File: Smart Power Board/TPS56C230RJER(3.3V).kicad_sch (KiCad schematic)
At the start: 19 parts, among them U5 TPS56C230RJER

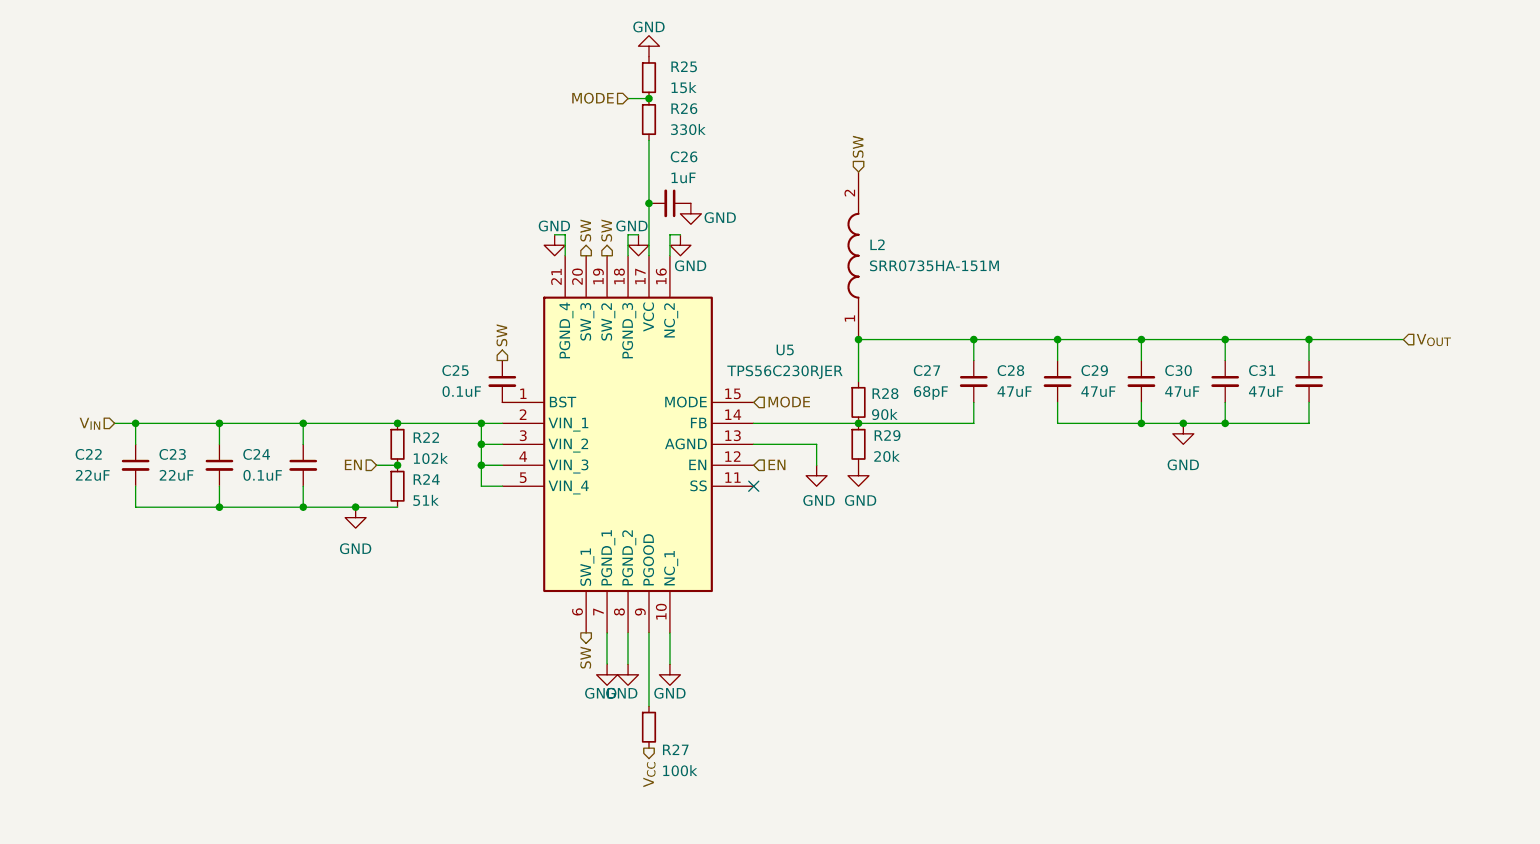
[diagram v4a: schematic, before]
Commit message: Feat[SmartPowerBoard]: Organized Schematic and New Buck
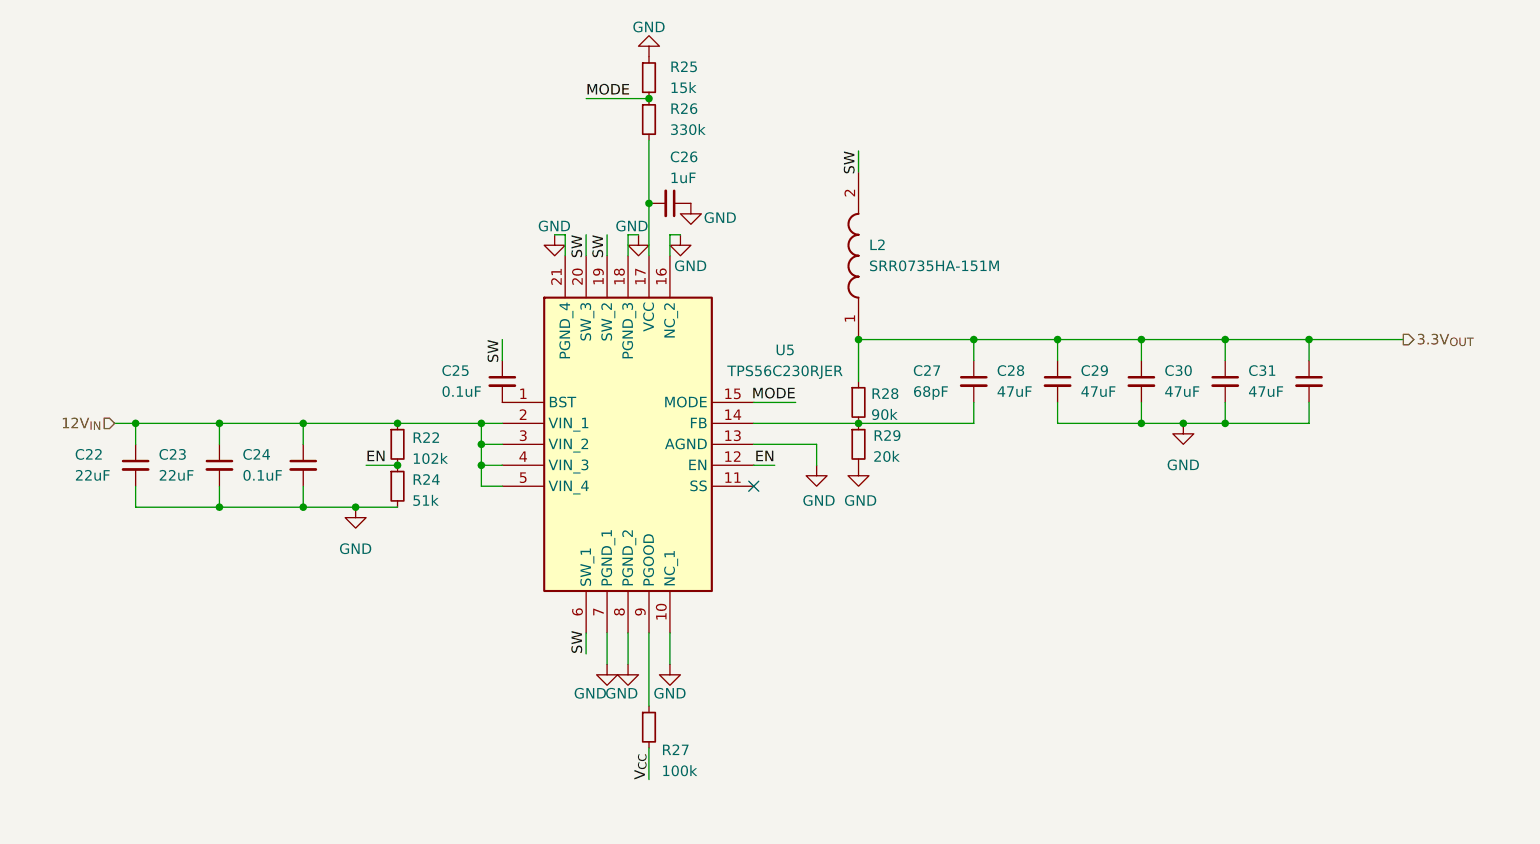
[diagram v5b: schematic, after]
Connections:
- net V_{IN} renamed 12V_{IN}
- net V_{OUT} renamed 3.3V_{OUT}
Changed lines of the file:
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@@
+	(wire
+		(pts
+			(xy 129.54 92.71) (xy 129.54 95.25)
+		)
+		(stroke
+			(width 0)
+			(type default)
+		)
+	)
 	(wire
 		(pts
@@
 	(wire
 		(pts
+			(xy 162.56 107.95) (xy 160.02 107.95)
+		)
+		(stroke
+			(width 0)
+			(type default)
+		)
+	)
+	(wire
+		(pts
 			(xy 142.24 128.27) (xy 142.24 132.08)
 		)
@@
 	(wire
 		(pts
-			(xy 144.78 63.5) (xy 147.32 63.5)
+			(xy 139.7 63.5) (xy 147.32 63.5)
 		)
 		(stroke
@@
 	(wire
 		(pts
+			(xy 165.1 100.33) (xy 160.02 100.33)
+		)
+		(stroke
+			(width 0)
+			(type default)
+		)
+	)
+	(wire
+		(pts
 			(xy 227.33 100.33) (xy 227.33 102.87)
 		)
@@
 	(wire
 		(pts
-			(xy 114.3 107.95) (xy 116.84 107.95)
+			(xy 113.03 107.95) (xy 116.84 107.95)
 		)
 		(stroke
@@
 	(wire
 		(pts
+			(xy 142.24 80.01) (xy 142.24 82.55)
+		)
+		(stroke
+			(width 0)
+			(type default)
+		)
+	)
+	(wire
+		(pts
+			(xy 139.7 80.01) (xy 139.7 82.55)
+		)
+		(stroke
+			(width 0)
+			(type default)
+		)
+	)
+	(wire
+		(pts
+			(xy 147.32 146.05) (xy 147.32 142.24)
+		)
+		(stroke
+			(width 0)
+			(type default)
+		)
+	)
+	(wire
+		(pts
 			(xy 196.85 100.33) (xy 196.85 102.87)
 		)
@@
 	(wire
 		(pts
+			(xy 139.7 130.81) (xy 139.7 128.27)
+		)
+		(stroke
+			(width 0)
+			(type default)
+		)
+	)
+	(wire
+		(pts
 			(xy 227.33 92.71) (xy 227.33 95.25)
 		)
@@
 	(wire
 		(pts
+			(xy 172.72 69.85) (xy 172.72 72.39)
+		)
+		(stroke
+			(width 0)
+			(type default)
+		)
+	)
+	(wire
+		(pts
 			(xy 137.16 80.01) (xy 137.16 82.55)
 		)
@@
 		)
 	)
-	(hierarchical_label "EN"
-		(shape input)
-		(at 114.3 107.95 180)
+	(label "SW"
+		(at 129.54 92.71 270)
 		(fields_autoplaced yes)
 		(effects
@@
 				(size 1.27 1.27)
 			)
-			(justify right)
-		)
-	)
-	(hierarchical_label "SW"
-		(shape input)
-		(at 172.72 72.39 90)
+			(justify right bottom)
+		)
+	)
+	(label "MODE"
+		(at 139.7 63.5 0)
 		(fields_autoplaced yes)
 		(effects
@@
 				(size 1.27 1.27)
 			)
-			(justify left)
-		)
-	)
-	(hierarchical_label "SW"
-		(shape output)
-		(at 139.7 82.55 90)
+			(justify left bottom)
+		)
+	)
+	(label "SW"
+		(at 142.24 80.01 270)
 		(fields_autoplaced yes)
 		(effects
@@
 				(size 1.27 1.27)
 			)
-			(justify left)
-		)
-	)
-	(hierarchical_label "EN"
-		(shape input)
-		(at 160.02 107.95 0)
+			(justify right bottom)
+		)
+	)
+	(label "SW"
+		(at 139.7 80.01 270)
 		(fields_autoplaced yes)
 		(effects
@@
 				(size 1.27 1.27)
 			)
-			(justify left)
-		)
-	)
-	(hierarchical_label "MODE"
-		(shape input)
-		(at 160.02 100.33 0)
+			(justify right bottom)
+		)
+	)
+	(label "SW"
+		(at 139.7 130.81 90)
 		(fields_autoplaced yes)
 		(effects
@@
 				(size 1.27 1.27)
 			)
-			(justify left)
-		)
-	)
-	(hierarchical_label "V_{CC}"
-		(shape output)
-		(at 147.32 142.24 270)
+			(justify left bottom)
+		)
+	)
+	(label "EN"
+		(at 162.56 107.95 180)
 		(fields_autoplaced yes)
 		(effects
@@
 				(size 1.27 1.27)
 			)
-			(justify right)
-		)
-	)
-	(hierarchical_label "MODE"
-		(shape input)
-		(at 144.78 63.5 180)
+			(justify right bottom)
+		)
+	)
+	(label "MODE"
+		(at 165.1 100.33 180)
 		(fields_autoplaced yes)
 		(effects
@@
 				(size 1.27 1.27)
 			)
-			(justify right)
-		)
-	)
-	(hierarchical_label "SW"
-		(shape output)
-		(at 129.54 95.25 90)
+			(justify right bottom)
+		)
+	)
+	(label "EN"
+		(at 113.03 107.95 0)
 		(fields_autoplaced yes)
 		(effects
@@
 				(size 1.27 1.27)
 			)
-			(justify left)
-		)
-	)
-	(hierarchical_label "SW"
-		(shape output)
-		(at 139.7 128.27 270)
+			(justify left bottom)
+		)
+	)
+	(label "V_{CC}"
+		(at 147.32 146.05 90)
 		(fields_autoplaced yes)
 		(effects
@@
 				(size 1.27 1.27)
 			)
-			(justify right)
-		)
-	)
-	(hierarchical_label "V_{IN}"
+			(justify left bottom)
+		)
+	)
+	(label "SW"
+		(at 172.72 69.85 270)
+		(fields_autoplaced yes)
+		(effects
+			(font
+				(size 1.27 1.27)
+			)
+			(justify right bottom)
+		)
+	)
+	(hierarchical_label "12V_{IN}"
 		(shape input)
 		(at 82.55 102.87 180)
@@
 		)
 	)
-	(hierarchical_label "V_{OUT}"
-		(shape input)
+	(hierarchical_label "3.3V_{OUT}"
+		(shape output)
 		(at 238.76 92.71 0)
-		(fields_autoplaced yes)
-		(effects
-			(font
-				(size 1.27 1.27)
-			)
-			(justify left)
-		)
-	)
-	(hierarchical_label "SW"
-		(shape output)
-		(at 142.24 82.55 90)
 		(fields_autoplaced yes)
 		(effects
@@
 		)
 		(property "Value" "GND"
-			(at 141.478 135.636 0)
-			(effects
-				(font
+			(at 140.208 135.636 0)
+			(effects
+				(font

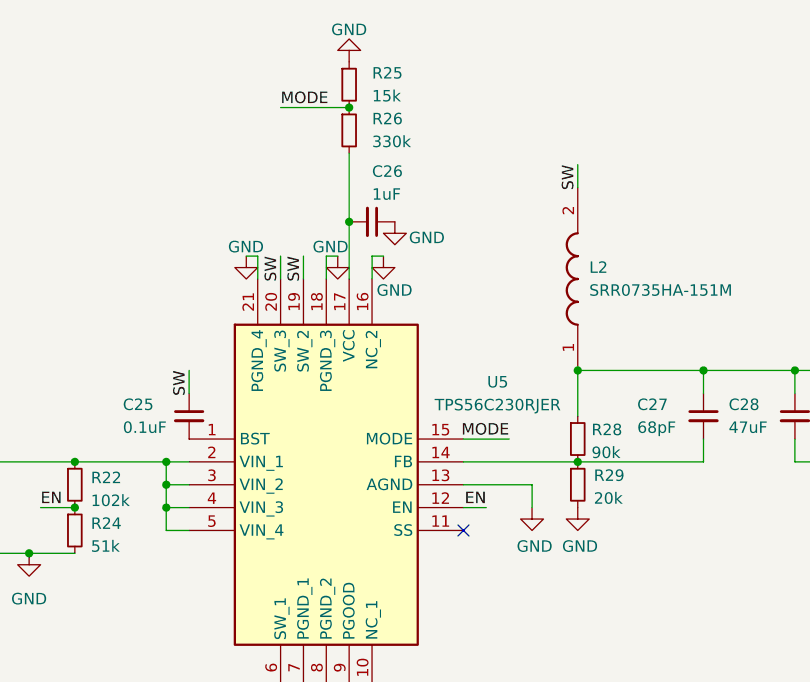
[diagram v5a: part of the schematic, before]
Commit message: Feat[SmartPowerBoard]: Routing
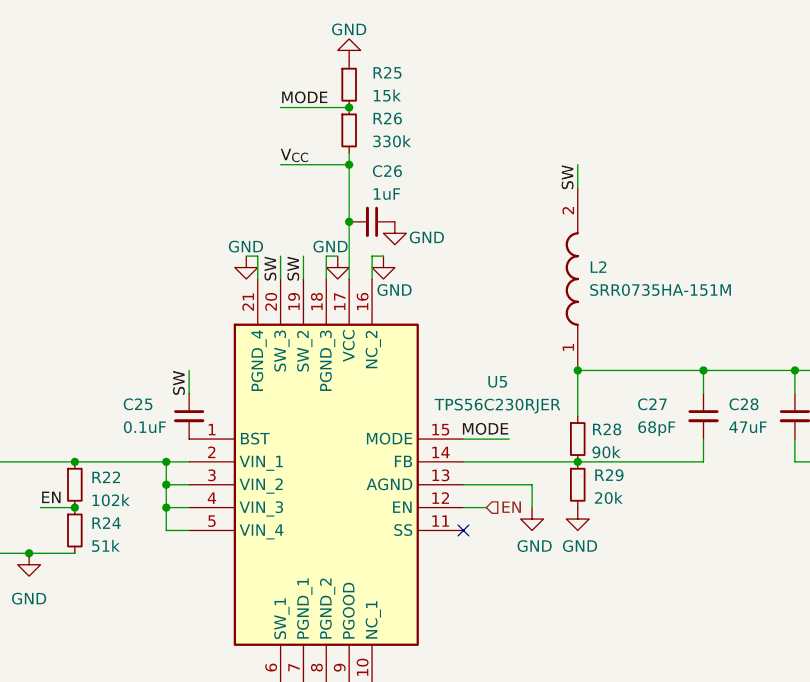
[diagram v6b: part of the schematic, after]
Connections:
- net V_{CC}: now also C26.2, R26.2, U5.17 (VCC)
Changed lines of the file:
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@@
+		(color 0 0 0 0)
+	)
+	(junction
+		(at 147.32 69.85)
+		(diameter 0)
 		(color 0 0 0 0)
 	)
@@
 	(wire
 		(pts
+			(xy 139.7 69.85) (xy 147.32 69.85)
+		)
+		(stroke
+			(width 0)
+			(type default)
+		)
+	)
+	(wire
+		(pts
 			(xy 147.32 137.16) (xy 147.32 128.27)
 		)
@@
 	(wire
 		(pts
-			(xy 147.32 68.58) (xy 147.32 76.2)
+			(xy 147.32 68.58) (xy 147.32 69.85)
 		)
 		(stroke
@@
 		(pts
 			(xy 139.7 80.01) (xy 139.7 82.55)
+		)
+		(stroke
+			(width 0)
+			(type default)
+		)
+	)
+	(wire
+		(pts
+			(xy 147.32 69.85) (xy 147.32 76.2)
 		)
 		(stroke
@@
 		)
 	)
+	(label "V_{CC}"
+		(at 139.7 69.85 0)
+		(fields_autoplaced yes)
+		(effects
+			(font
+				(size 1.27 1.27)
+			)
+			(justify left bottom)
+		)
+	)
 	(label "MODE"
 		(at 139.7 63.5 0)
@@
 		)
 	)
-	(label "EN"
-		(at 162.56 107.95 180)
-		(fields_autoplaced yes)
-		(effects
-			(font
-				(size 1.27 1.27)
-			)
-			(justify right bottom)
-		)
-	)
 	(label "MODE"
 		(at 165.1 100.33 180)
@@
 		)
 	)
+	(hierarchical_label "EN"
+		(shape input)
+		(at 162.56 107.95 0)
+		(fields_autoplaced yes)
+		(effects
+			(font
+				(size 1.27 1.27)
+			)
+			(justify left)
+		)
+	)

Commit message: Feat[SmartPowerBoard]: Silkscreen + Ground
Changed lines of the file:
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@@
 (kicad_sch
-	(version 20240101)
+	(version 20241004)
 	(generator "eeschema")
 	(generator_version "8.99")

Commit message: Feat[SmartPowerBoard]: Tapeout
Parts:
- C22, C23, C28, C29, C30, C31: footprint Capacitor_SMD:C_0402_1005Metric -> Capacitor_SMD:C_0603_1608Metric
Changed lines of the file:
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@@
 			)
 		)
-		(property "Footprint" "Capacitor_SMD:C_0402_1005Metric"
+		(property "Footprint" "Capacitor_SMD:C_0603_1608Metric"
 			(at 196.85 97.79 0)
 			(effects
@@
 			)
 		)
-		(property "Footprint" "Capacitor_SMD:C_0402_1005Metric"
+		(property "Footprint" "Capacitor_SMD:C_0603_1608Metric"
 			(at 85.09 107.95 0)
 			(effects
@@
 			)
 		)
-		(property "Footprint" "Capacitor_SMD:C_0402_1005Metric"
+		(property "Footprint" "Capacitor_SMD:C_0603_1608Metric"
 			(at 95.25 107.95 0)
 			(effects
@@
 			)
 		)
-		(property "Footprint" "Capacitor_SMD:C_0402_1005Metric"
+		(property "Footprint" "Capacitor_SMD:C_0603_1608Metric"
 			(at 207.01 97.79 0)
 			(effects
@@
 			)
 		)
-		(property "Footprint" "Capacitor_SMD:C_0402_1005Metric"
+		(property "Footprint" "Capacitor_SMD:C_0603_1608Metric"
 			(at 227.33 97.79 0)
 			(effects
@@
 			)
 		)
-		(property "Footprint" "Capacitor_SMD:C_0402_1005Metric"
+		(property "Footprint" "Capacitor_SMD:C_0603_1608Metric"
 			(at 217.17 97.79 0)
 			(effects
